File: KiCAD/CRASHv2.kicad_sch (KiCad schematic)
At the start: 4 parts, among them U1 ATmega32A-A, U2 LM317_SOT-223

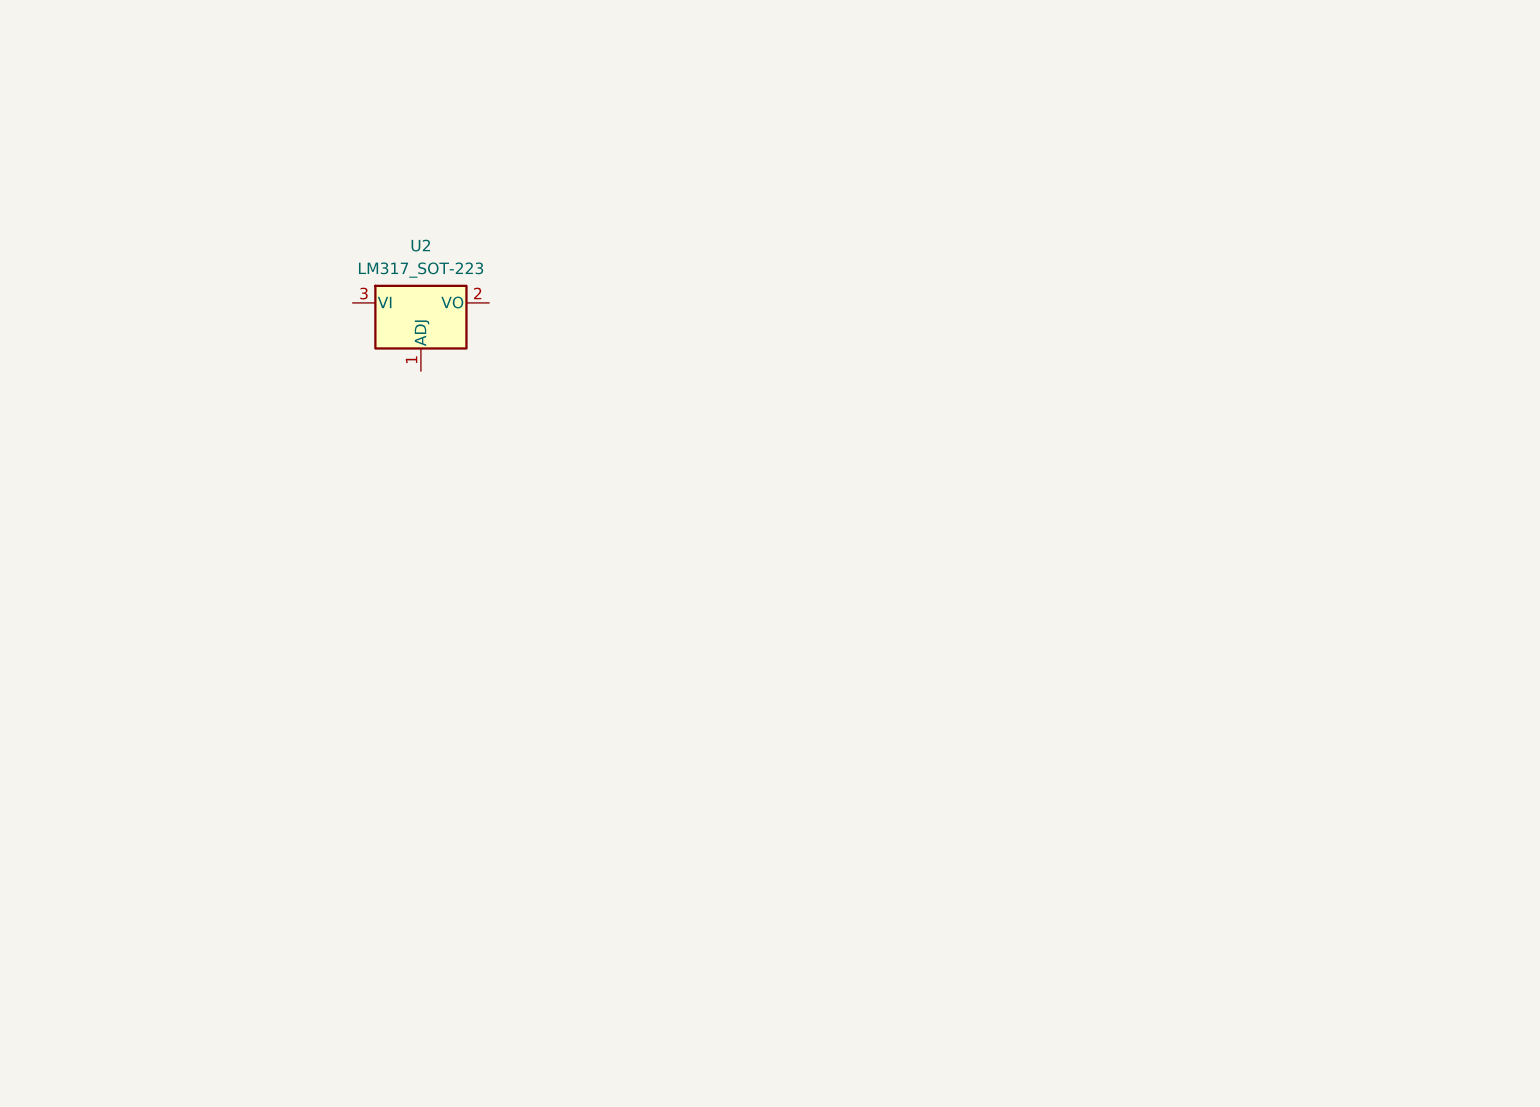
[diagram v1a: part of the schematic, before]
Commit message: USB interface + start of nrf24 probably gonna have to swap nrf24 to an external component
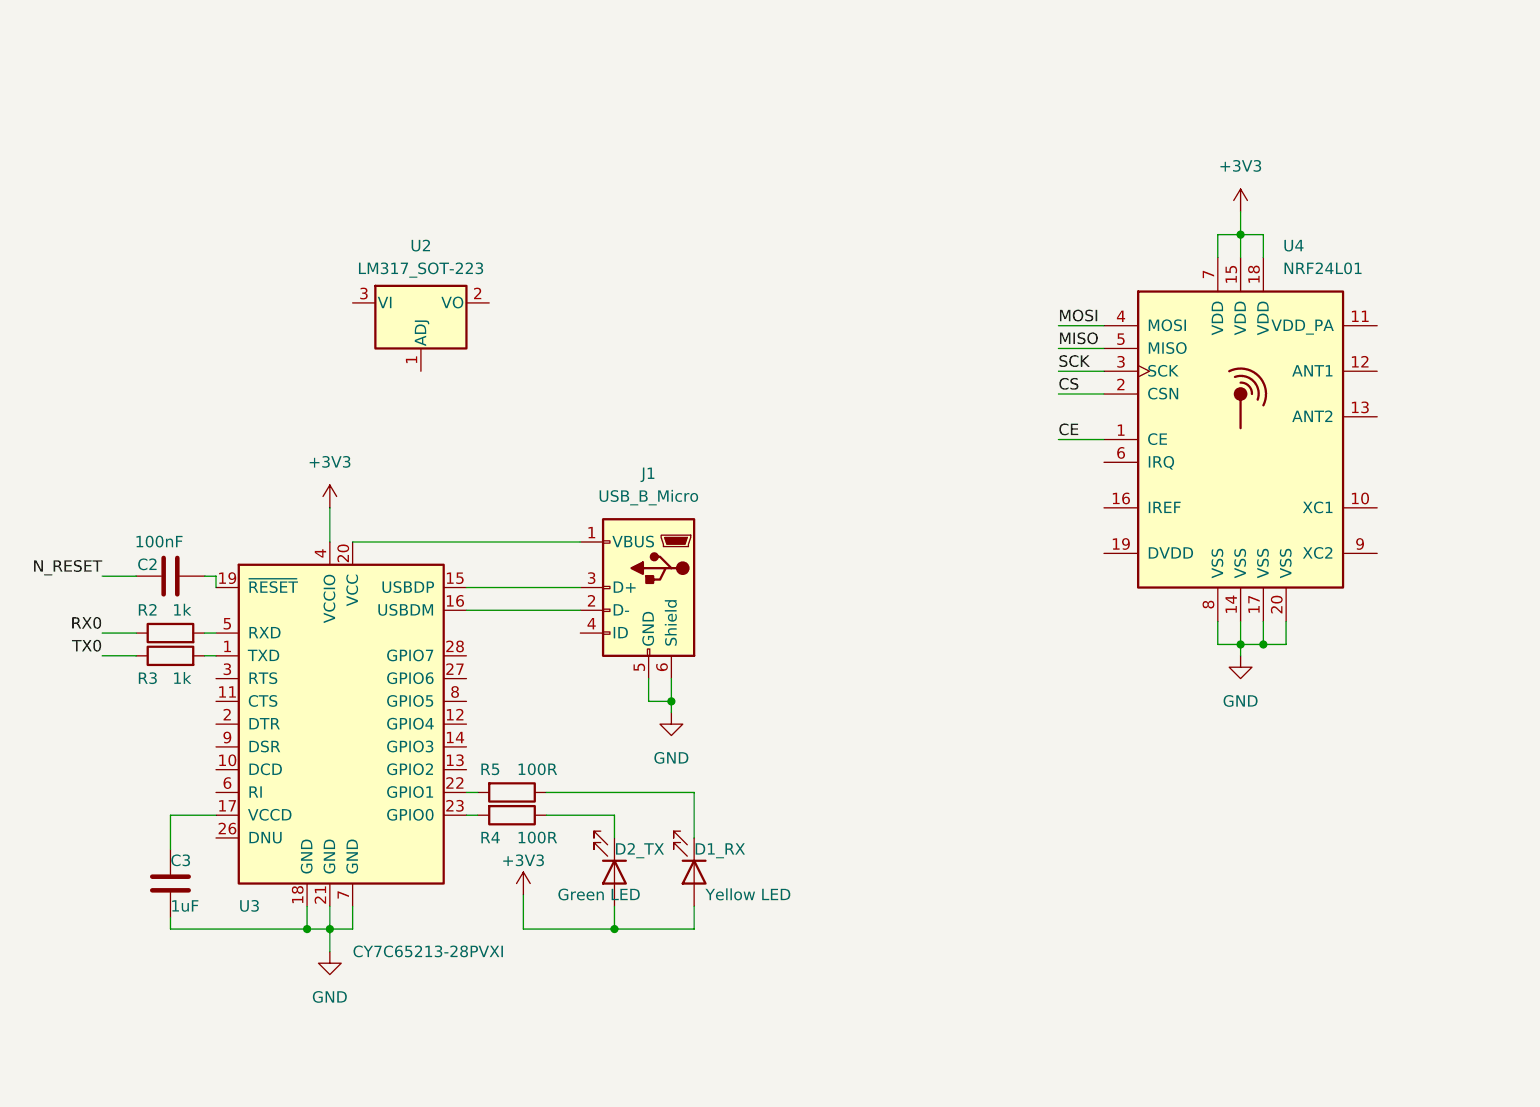
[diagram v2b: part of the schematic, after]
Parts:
- added C2: 100nF, symbol Device:C
- added C3: 1uF, symbol Device:C
- added D1_RX: Yellow LED, symbol Device:LED
- added D2_TX: Green LED, symbol Device:LED
- added J1: USB_B_Micro, symbol Connector:USB_B_Micro
- added R2, R3: 1k, symbol Device:R
- added R4, R5: 100R, symbol Device:R
- added U3: CY7C65213-28PVXI, Package_SO:SSOP-28_5.3x10.2mm_P0.65mm, symbol Interface_USB:CY7C65213-28PVXI
- added U4: NRF24L01, Package_DFN_QFN:QFN-20-1EP_4x4mm_P0.5mm_EP2.5x2.5mm, symbol RF:NRF24L01
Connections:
- net CE: now also U4.1 (CE)
- net CS: now also U4.2 (CSN)
- net GND: now also C3.2, J1.5 (GND), J1.6 (Shield), U3.18 (GND), U3.21 (GND), U3.7 (GND), U4.14 (VSS), U4.17 (VSS), U4.20 (VSS), U4.8 (VSS)
- net MISO: now also U4.5 (MISO)
- net MOSI: now also U4.4 (MOSI)
- net N_RESET: now also C2.1
- net RX0: now also R2.1
- net SCK: now also U4.3 (SCK)
- net TX0: now also R3.1
- new net: J1.1 (VBUS), U3.20 (VCC)
- new net: J1.2 (D-), U3.16 (USBDM)
- new net: J1.3 (D+), U3.15 (USBDP)
- new net: D1_RX.1 (K), R5.1
- new net: R3.2, U3.1 (TXD)
- new net: R2.2, U3.5 (RXD)
- new net: C3.1, U3.17 (VCCD)
- new net: C2.2, U3.19 (~{RESET})
- new net: R5.2, U3.22 (GPIO1)
- new net: R4.2, U3.23 (GPIO0)
- new net: D2_TX.1 (K), R4.1
- new net +3V3: D1_RX.2 (A), D2_TX.2 (A), U3.4 (VCCIO), U4.15 (VDD), U4.18 (VDD), U4.7 (VDD)

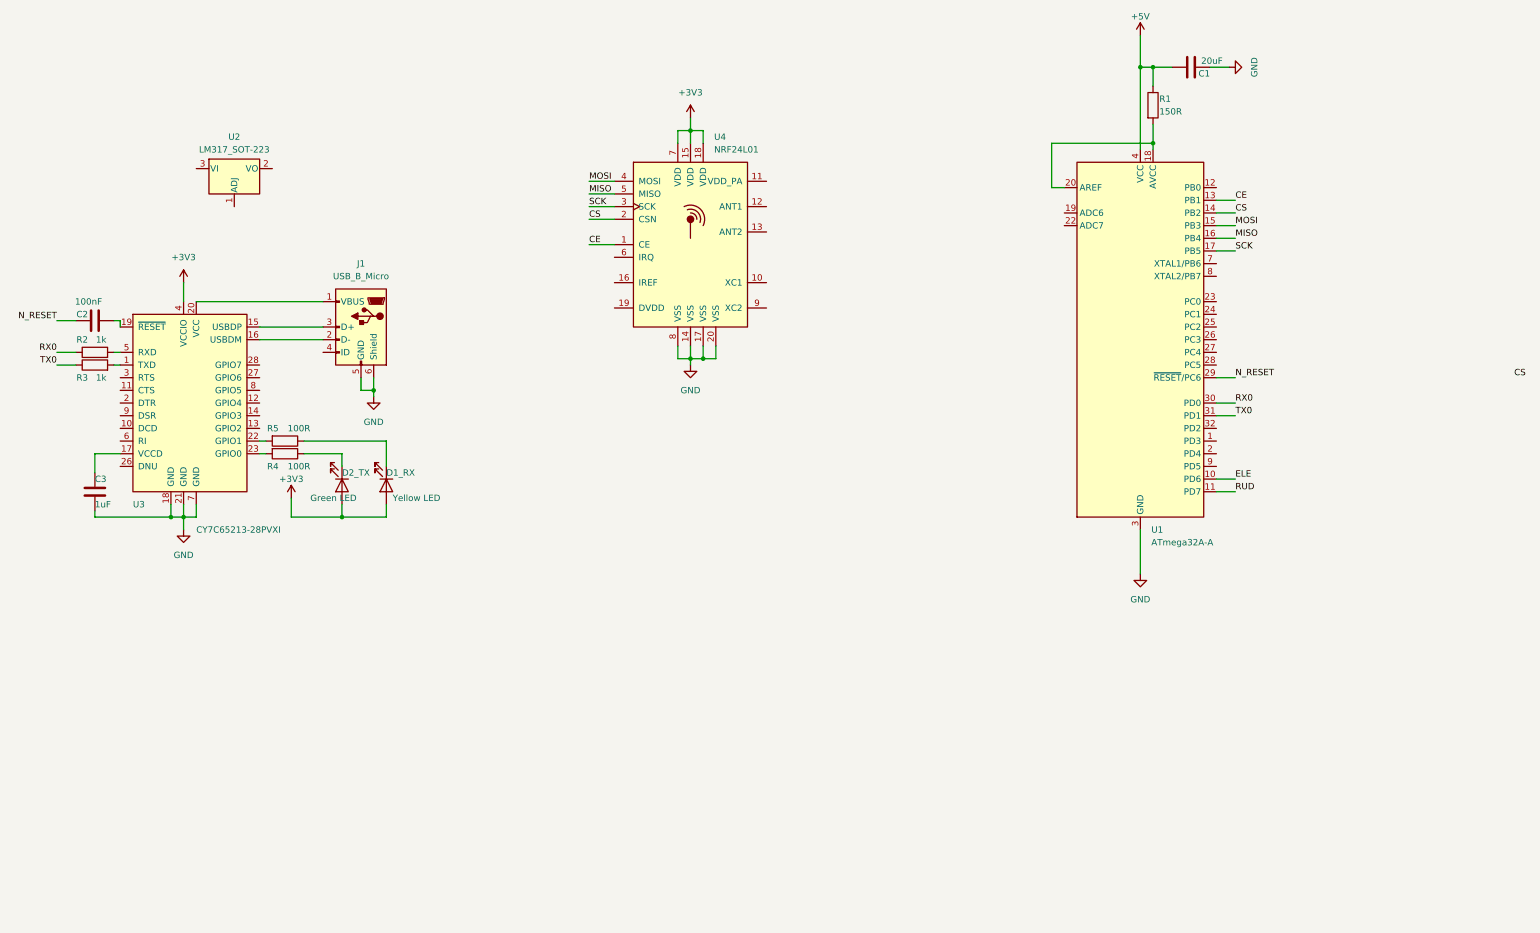
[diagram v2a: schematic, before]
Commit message: Rearrange components and start on power supply Power supply stolen from BINGU v0.4
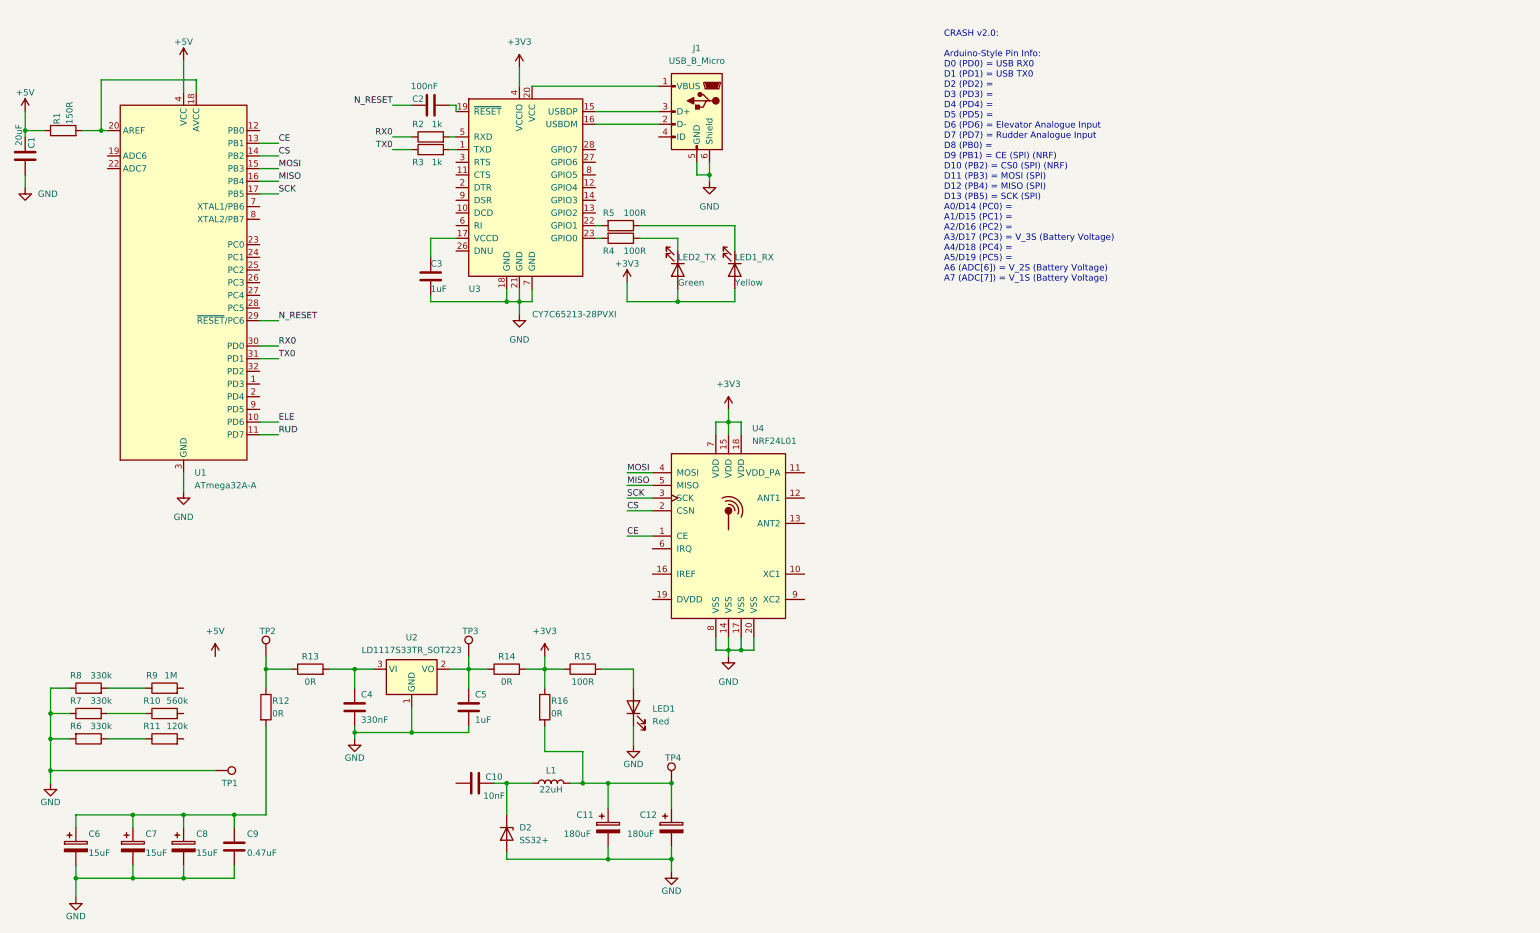
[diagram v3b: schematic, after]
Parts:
- removed U2: LM317_SOT-223, Package_TO_SOT_SMD:SOT-223-3_TabPin2, symbol Regulator_Linear:LM317_SOT-223
- added C10: 10nF, symbol Device:C
- added C11, C12: 180uF, symbol Device:C_Polarized
- added C4: 330nF, symbol Device:C
- added C5: 1uF, symbol Device:C
- added C6, C7, C8: 15uF, symbol Device:C_Polarized
- added C9: 0.47uF, symbol Device:C
- added D2: SS32+, symbol Device:D_Zener
- added L1: 22uH, symbol Device:L
- added LED1: Red, symbol Device:LED
- added R10: 560k, symbol Device:R
- added R11: 120k, symbol Device:R
- added R12, R13, R14, R16: 0R, symbol Device:R
- added R15: 100R, symbol Device:R
- added R6, R7, R8: 330k, symbol Device:R
- added R9: 1M, symbol Device:R
- added TP1, TP2, TP3, TP4: TestPoint, symbol Connector:TestPoint
- added U2: LD1117S33TR_SOT223, Package_TO_SOT_SMD:SOT-223-3_TabPin2, symbol Regulator_Linear:LD1117S33TR_SOT223
- LED1_RX: renamed from D1_RX; value Yellow LED -> Yellow
- LED2_TX: renamed from D2_TX; value Green LED -> Green
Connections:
- net +3V3: now also R14.2, R15.1, R16.1
- net +5V: now also C1.2; no longer C1.1
- net GND: now also C1.1, C11.2, C12.2, C4.2, C5.2, C6.2, C7.2, C8.2, C9.2, D2.2 (A), LED1.1 (K), R6.2, R7.1, R8.1, TP1.1, U2.1 (GND); no longer C1.2
- new net: R12.1, R13.1, TP2.1
- new net: C4.1, R13.2, U2.3 (VI)
- new net: LED1.2 (A), R15.2
- new net: C11.1, C12.1, L1.2, R16.2, TP4.1
- new net: R10.1, R7.2
- new net: R8.2, R9.1
- new net: R11.1, R6.1
- new net: C10.2, D2.1 (K), L1.1
- new net: C6.1, C7.1, C8.1, C9.1, R12.2
- new net: C5.1, R14.1, TP3.1, U2.2 (VO)
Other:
- note added: "CRASH v2.0: Arduino-Style Pin Info: D0 (PD0) = USB RX0 D1 (PD1) = USB TX0 D2 (PD2) = D3 (PD3) = D4 (PD4) = D5 (PD5) = D6 (PD6) = Elevator Analogue Input D7 (PD7) = Rudder Analogue Input D8 (PB0) = D9 (PB1) = CE (SPI) (NRF) D10 (PB2) = CS0 (SPI) (NRF) D11 (PB3) = MOSI (SPI) D12 (PB4) = MISO (SPI) D13 (PB5) = SCK (SPI) A0/D14 (PC0) = A1/D15 (PC1) = A2/D16 (PC2) = A3/D17 (PC3) = V_3S (Battery Voltag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"
- moved on the sheet: C1, C2, C3, J1, LED1_RX, LED2_TX, R1, R2, R3, R4, R5, U1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
